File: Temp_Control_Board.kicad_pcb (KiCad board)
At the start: 4 copper layers, 50.8 x 53.3 mm, 50 parts, among them J1 OVEN_INTERFACE, J2 OLED, J3 USB_B_Micro, J4 MICROSD, J5 BREAKOUT, Q1 BC847BS, SW1 BOOT, SW2 EN, U1 ESP-WROOM-32, U2 AZ1117EH-3.3TRG1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

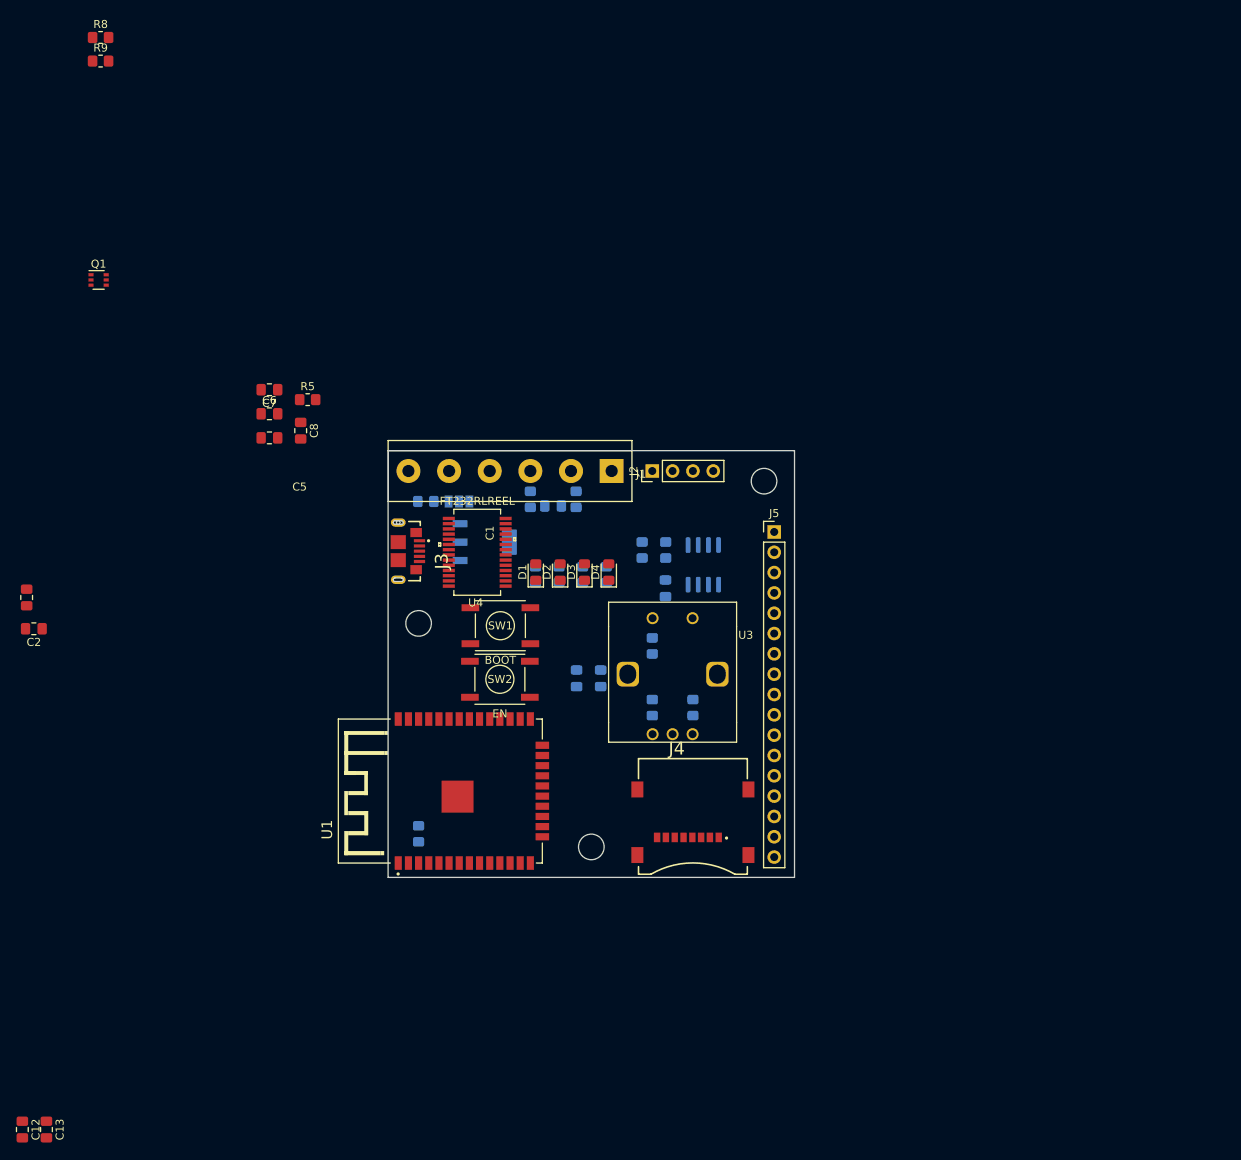
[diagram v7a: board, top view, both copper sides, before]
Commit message: pcb: components placed
    - sch: fixed FT_CTS -> FT_RTS on reset circuit
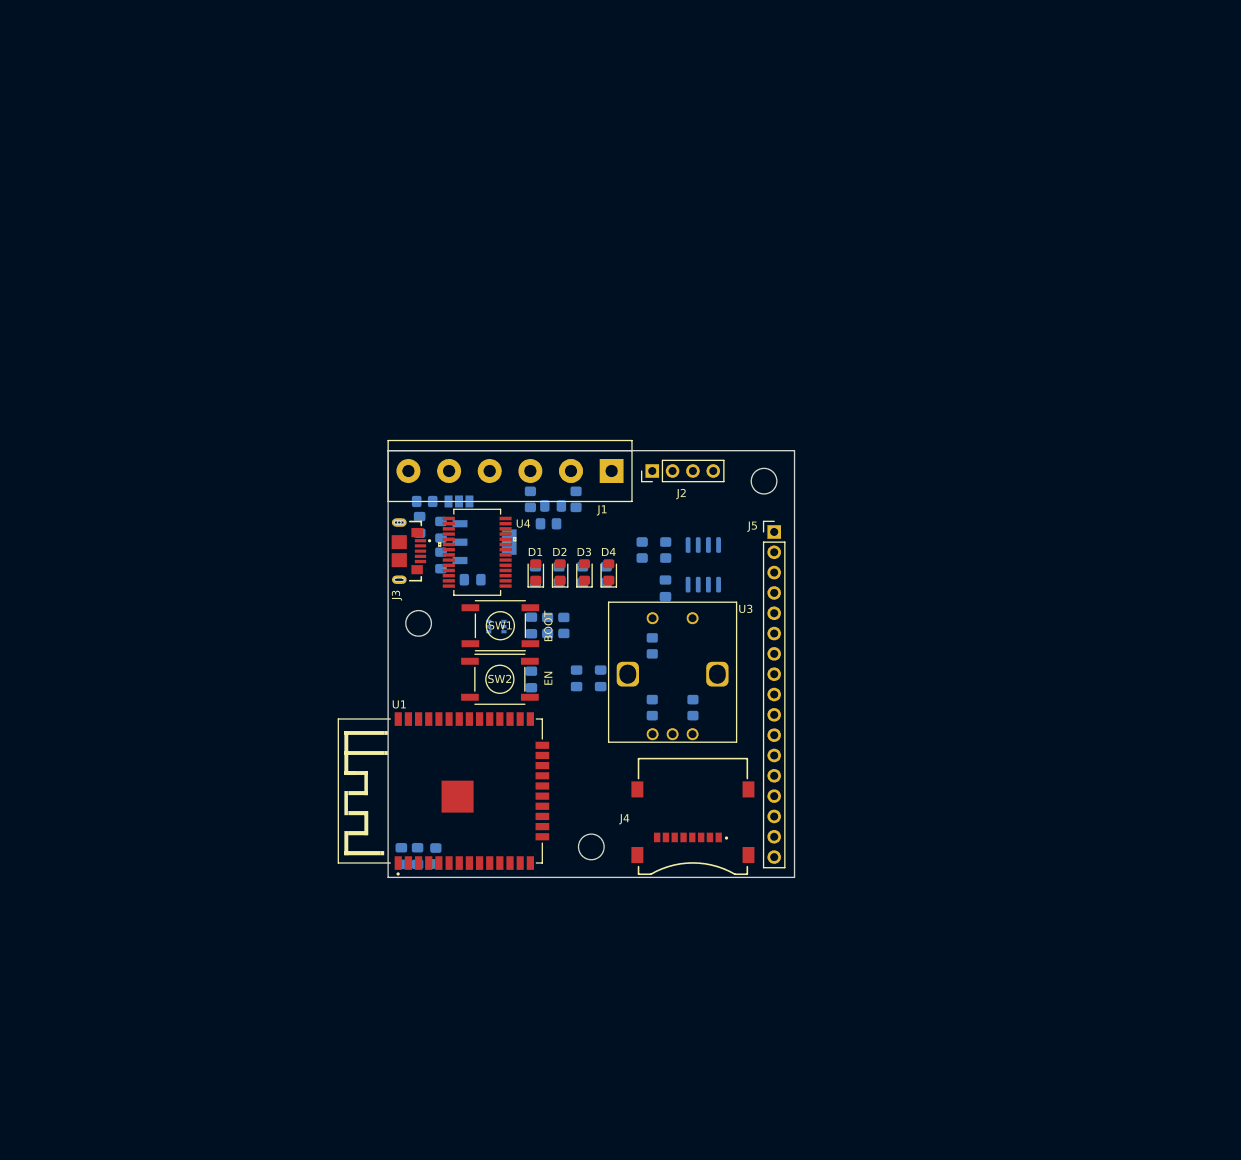
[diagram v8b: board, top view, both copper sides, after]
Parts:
- C1, C12, C13, C2, C5, C6, C7, C8, Q1, R5, R8, R9: moved to B.Cu
- moved R8 93.6 mm to (98.2, 120.9), turned to 90 degrees
- moved R9 90.0 mm to (96.1, 120.9), turned to -90 degrees
- moved Q1 65.9 mm to (89.7, 121.0), turned to 180 degrees
- moved C1 63.2 mm to (94.1, 120.9)
- moved C2 62.5 mm to (94.1, 127.7), turned to 90 degrees
- moved C12 60.1 mm to (79.9, 149.7), turned to 90 degrees
- moved C13 56.0 mm to (77.9, 149.7), turned to 90 degrees
- moved R5 33.9 mm to (96.2, 108.2)
- moved C7 30.2 mm to (82.8, 112.8), turned to -90 degrees
- moved C8 28.4 mm to (86.8, 115.2), turned to 0 degrees
- moved C5 24.3 mm to (82.8, 108.9), turned to 90 degrees
- moved C6 23.3 mm to (80.1, 108.3), turned to -90 degrees
- moved R1 3.52 mm to (82.2, 149.7), turned to 90 degrees
- moved G*** 3.08 mm to (85.9, 141.7)
- moved FB1 0.14 mm to (80.8, 105.4)
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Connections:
- Q1 pad 4: FT_CTS -> FT_RTS
- R9 pad 1: FT_CTS -> FT_RTS
